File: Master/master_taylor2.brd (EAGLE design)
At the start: 67.9 x 65.1 mm, 47 parts, among them J1 ISP, K1 653002114822, K2 653002114822, K3 653002114822, K4 653002114822, U1 ATMEGA128RFA1, U2 TPS73633-DBVT, U3 ULN2003ADR, Y1 16MHz

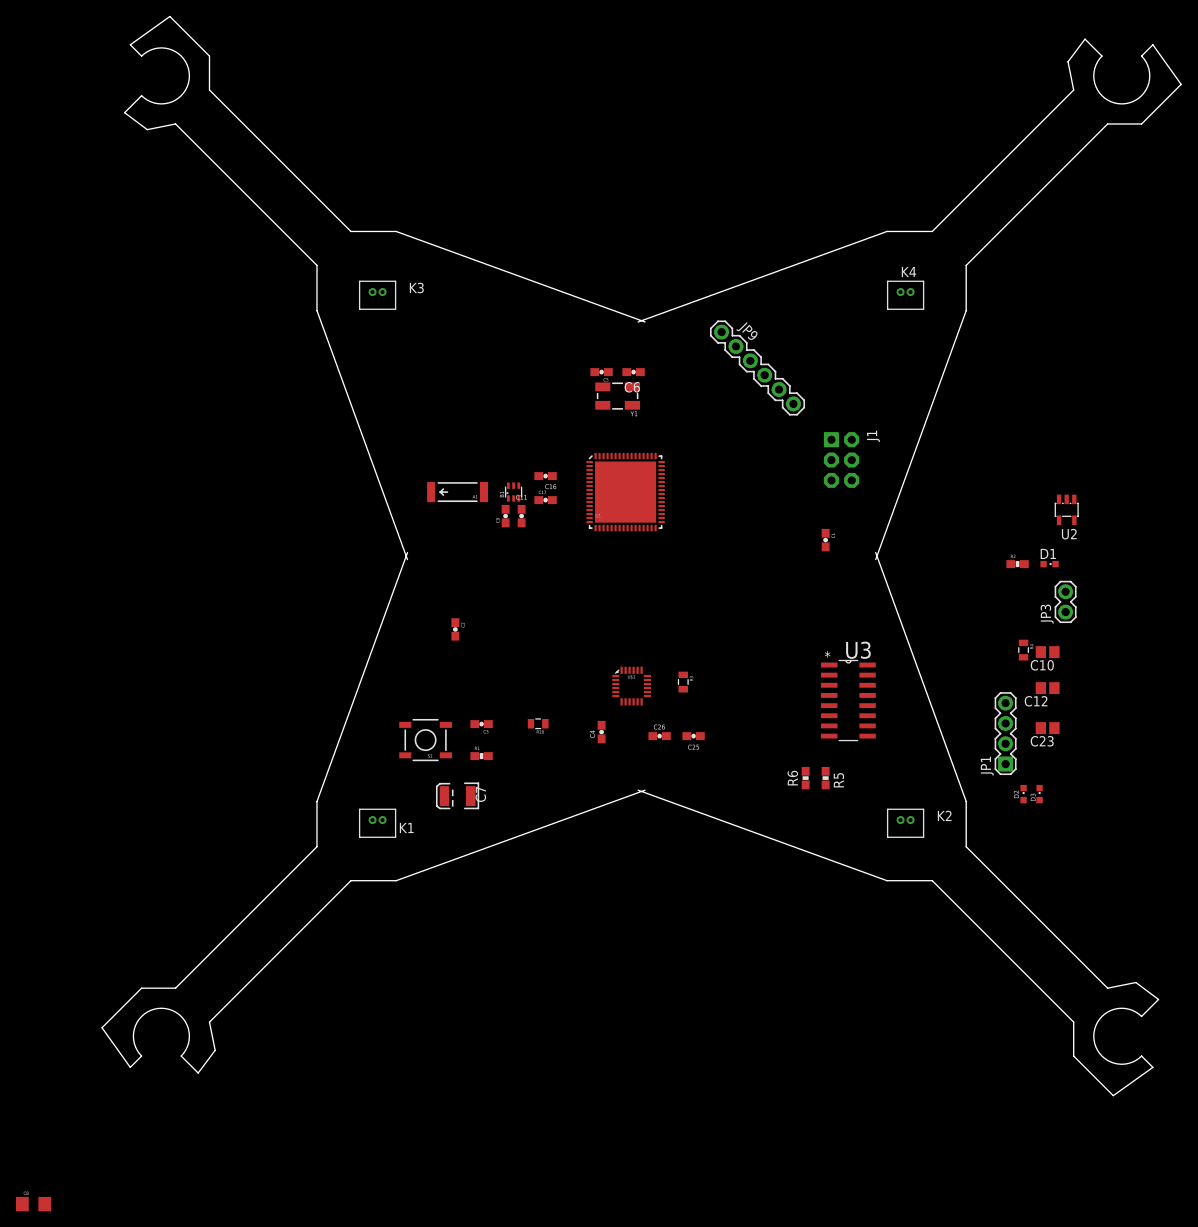
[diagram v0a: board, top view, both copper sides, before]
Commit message: Version 2 routed
Layed out crystal and antenna in accordance with the Cult of Sparkfun
Added keepouts to IMU because of Jorge's recommendation
Added keepout to antenna to not disturb the ether wind.
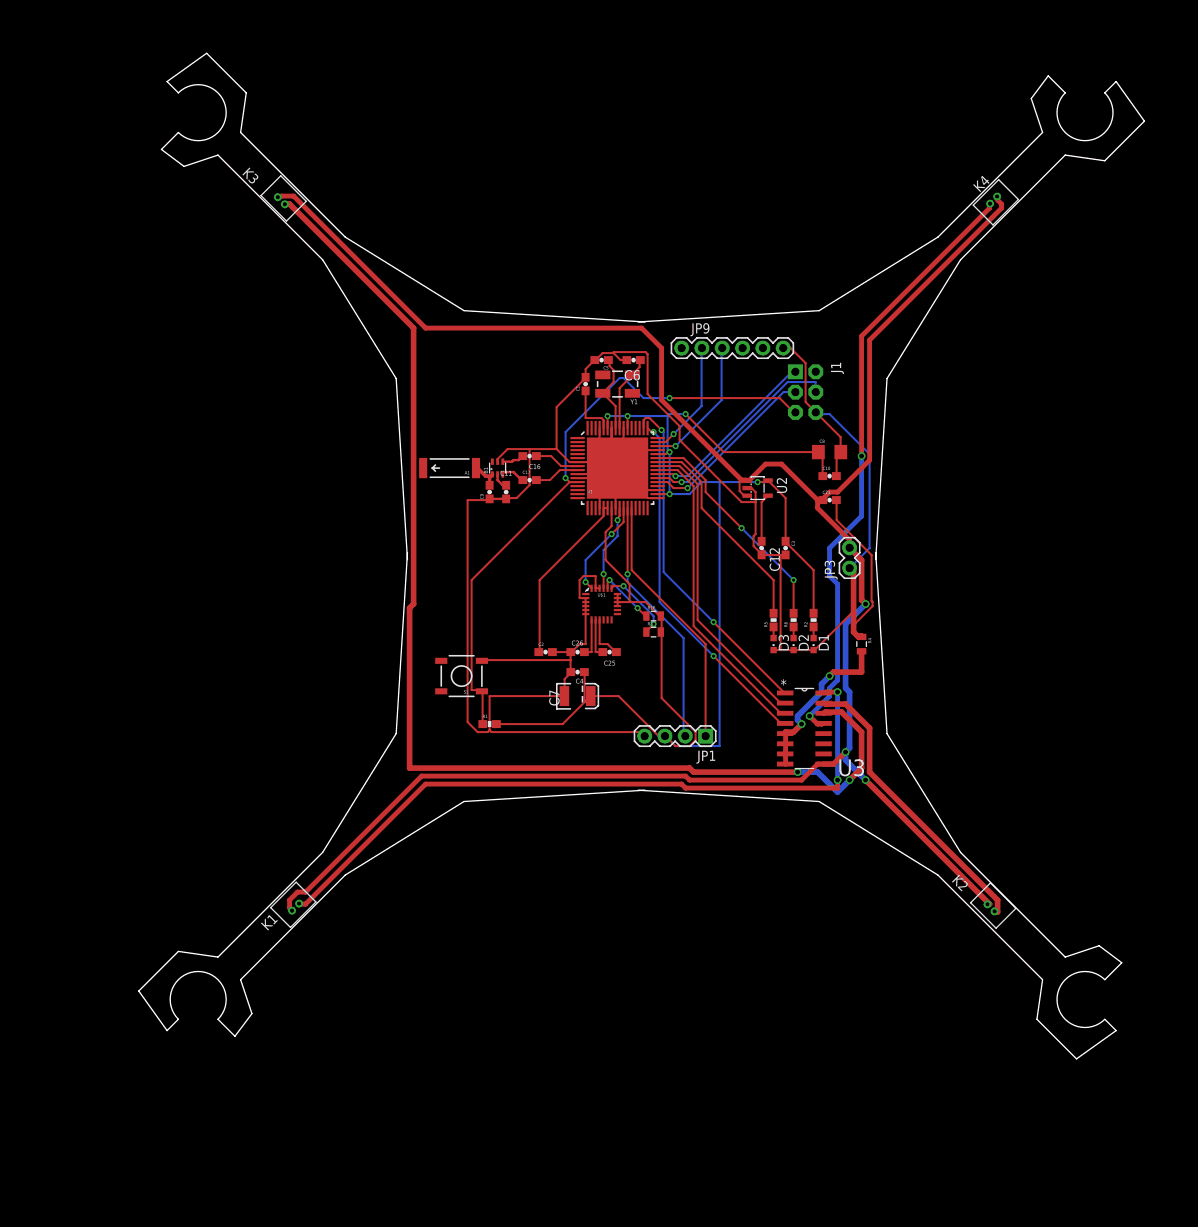
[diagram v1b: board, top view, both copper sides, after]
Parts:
- C10, C12, C23: device resistor:C0805 -> SparkFun-Capacitors:0603-CAP
- D3: value WHITE -> GREEN
- JP1: value Debuger -> Debugger
- U1: device SparkFun-DigitalIC:QFN-64 -> master_devon:QFN-64
- moved C8 136.9 mm to (23.5, 13.0)
- moved C3 43.9 mm to (18.0, 1.00), turned to 270 degrees
- moved C12 39.8 mm to (15.0, 1.00), turned to 270 degrees
- moved C23 39.4 mm to (23.5, 7.00), turned to 0 degrees
- moved U2 38.7 mm to (14.5, 8.50), turned to 270 degrees
- moved D3 38.2 mm to (16.5, -11.0), turned to 180 degrees
- moved JP1 37.7 mm to (8.00, -22.5), turned to 180 degrees
- moved C1 35.8 mm to (-7.00, 21.5), turned to 90 degrees
- moved C10 35.0 mm to (23.5, 10.0), turned to 0 degrees
- moved D2 34.3 mm to (19.0, -11.0), turned to 180 degrees
- moved D1 31.1 mm to (21.5, -11.0), turned to 180 degrees
- moved JP3 27.6 mm to (26.0, -1.50)
- moved R2 26.4 mm to (21.5, -8.00), turned to 90 degrees
- moved R5 20.8 mm to (16.5, -8.00), turned to 90 degrees
- moved R4 20.3 mm to (27.5, -11.0)
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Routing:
- net GND: track 0.00 -> 325.3 mm
- net VBAT: track 0.00 -> 281.3 mm, vias 0 -> 3
- net 3.3V: track 0.00 -> 191.8 mm, vias 0 -> 6
- net N$31: track 0.00 -> 147.0 mm, vias 0 -> 2
- net N$29: track 0.00 -> 87.5 mm, vias 0 -> 2
- net RESET: track 0.00 -> 77.4 mm, vias 0 -> 2
- net N$32: track 0.00 -> 76.4 mm, vias 0 -> 2
- net PE3: track 0.00 -> 44.5 mm, vias 0 -> 2
- net PE4: track 0.00 -> 43.3 mm, vias 0 -> 2
- net PB4: track 0.00 -> 38.8 mm
- net PB5: track 0.00 -> 38.2 mm
- net N$30: track 0.00 -> 37.0 mm
- net TX1: track 0.00 -> 32.3 mm
- net RX1: track 0.00 -> 31.6 mm, vias 0 -> 1
- net PB7: track 0.00 -> 28.3 mm, vias 0 -> 2
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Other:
- board size 67.9 x 65.1 mm -> 63.3 x 60.5 mm

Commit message: Changed outline a bit to reduce weight
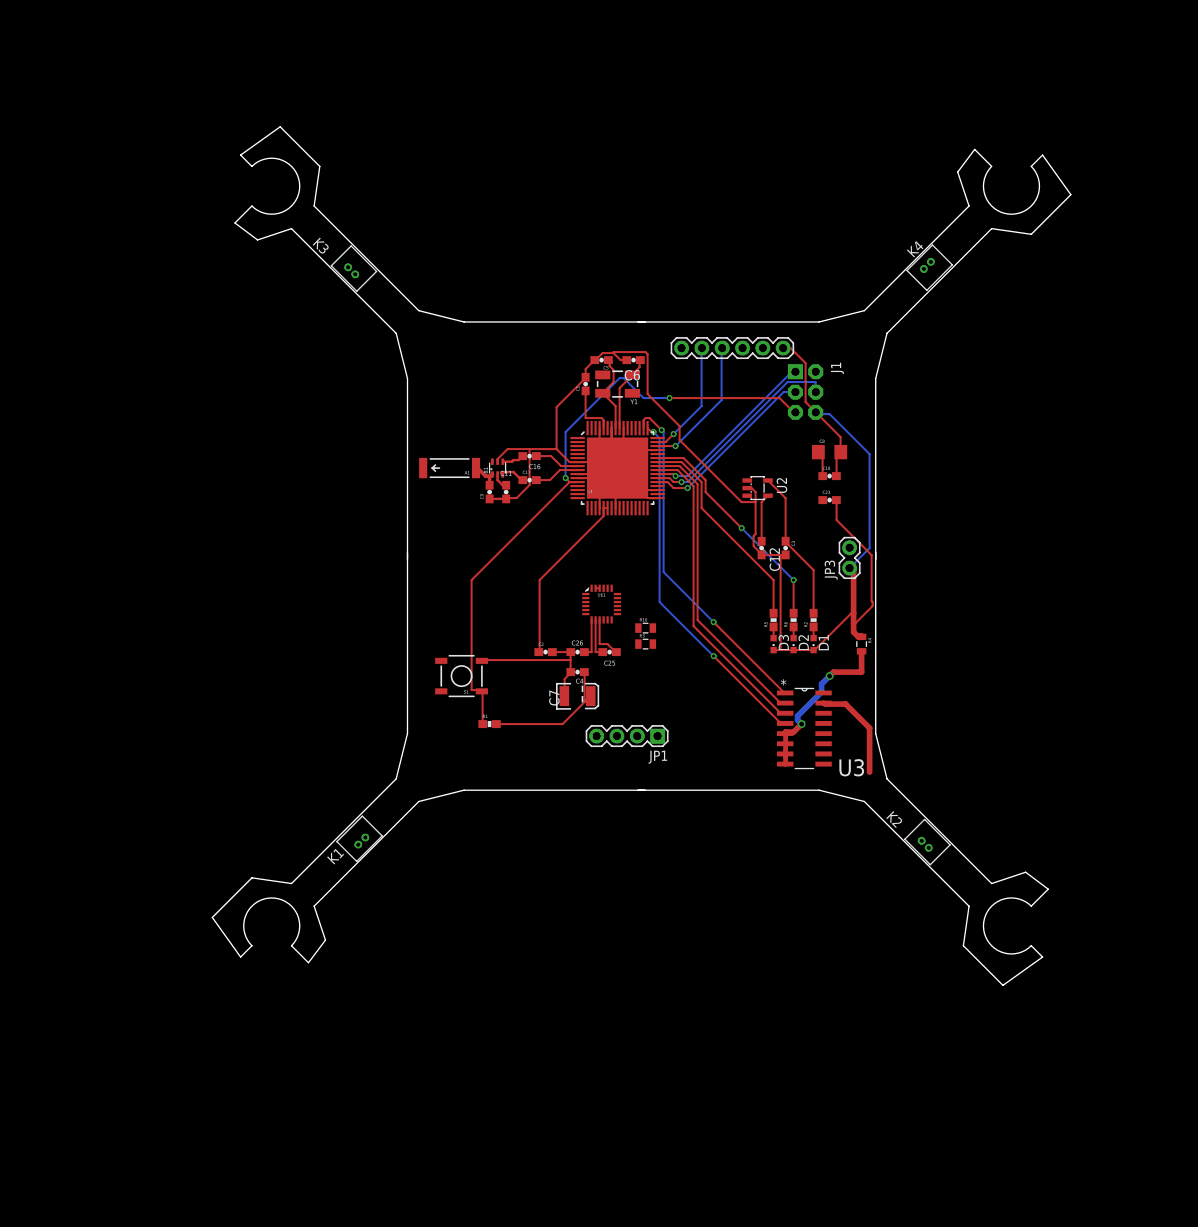
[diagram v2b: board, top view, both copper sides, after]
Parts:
- moved K3 12.4 mm to (-36.2, 35.7)
- moved K1 11.7 mm to (-35.0, -35.6)
- moved K4 11.6 mm to (35.7, 36.3)
- moved K2 11.4 mm to (35.5, -36.0)
- moved JP1 6.00 mm to (2.00, -22.5)
- moved R10 1.80 mm to (0.50, -9.00)
- moved R3 1.80 mm to (0.50, -11.0)
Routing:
- net VBAT: track 281.3 -> 0.00 mm, vias 3 -> 0
- net 3.3V: track 191.8 -> 39.2 mm, vias 6 -> 0
- net N$31: track 147.0 -> 0.00 mm, vias 2 -> 0
- net N$29: track 87.5 -> 0.00 mm, vias 2 -> 0
- net GND: track 325.3 -> 243.1 mm
- net N$32: track 76.4 -> 0.00 mm, vias 2 -> 0
- net TX1: track 32.3 -> 0.00 mm
- net RX1: track 31.6 -> 0.00 mm, vias 1 -> 0
- net N$30: track 37.0 -> 12.5 mm
- net SDA: track 12.3 -> 0.00 mm, vias 2 -> 0
- net SCL: track 10.9 -> 0.00 mm, vias 2 -> 0
- net N$23: track 9.45 -> 0.00 mm, vias 2 -> 0
- net N$24: track 7.74 -> 0.00 mm, vias 2 -> 0
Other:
- board size 63.3 x 60.5 mm -> 54.1 x 51.3 mm

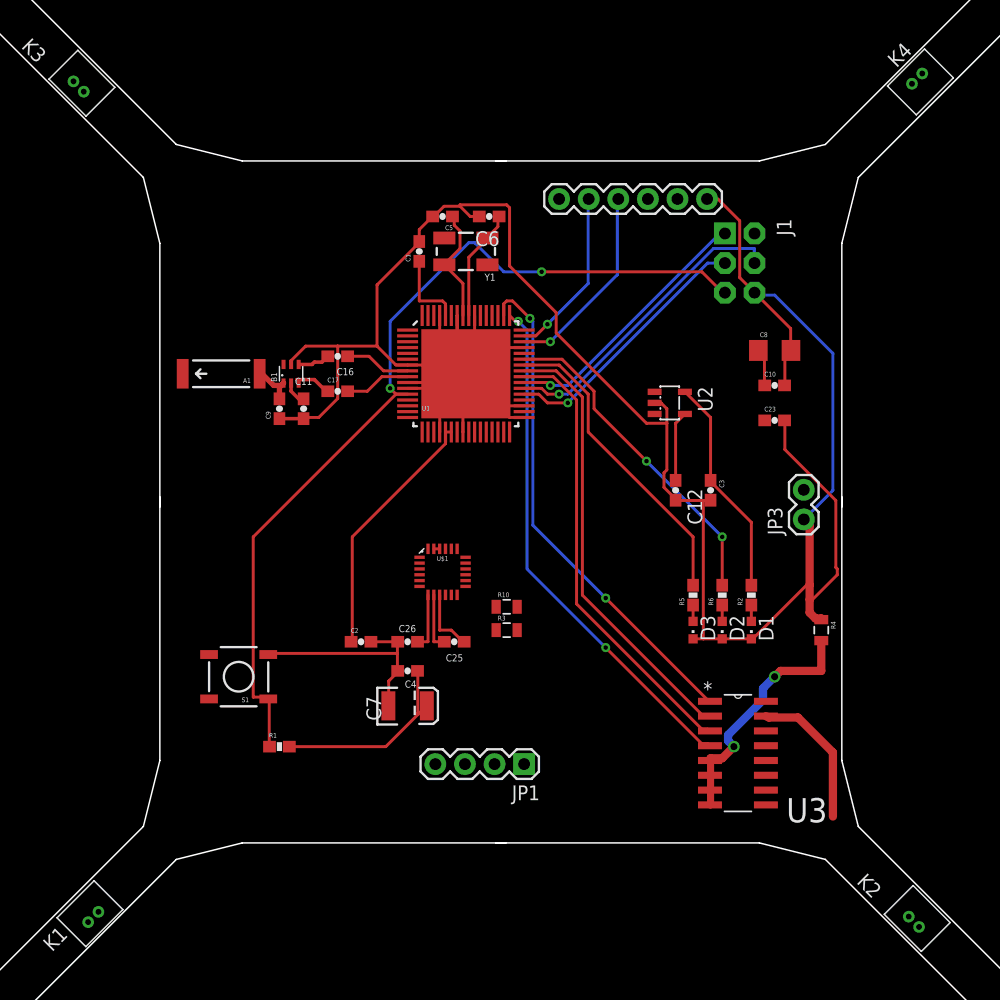
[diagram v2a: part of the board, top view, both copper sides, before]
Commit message: Hand routed motors
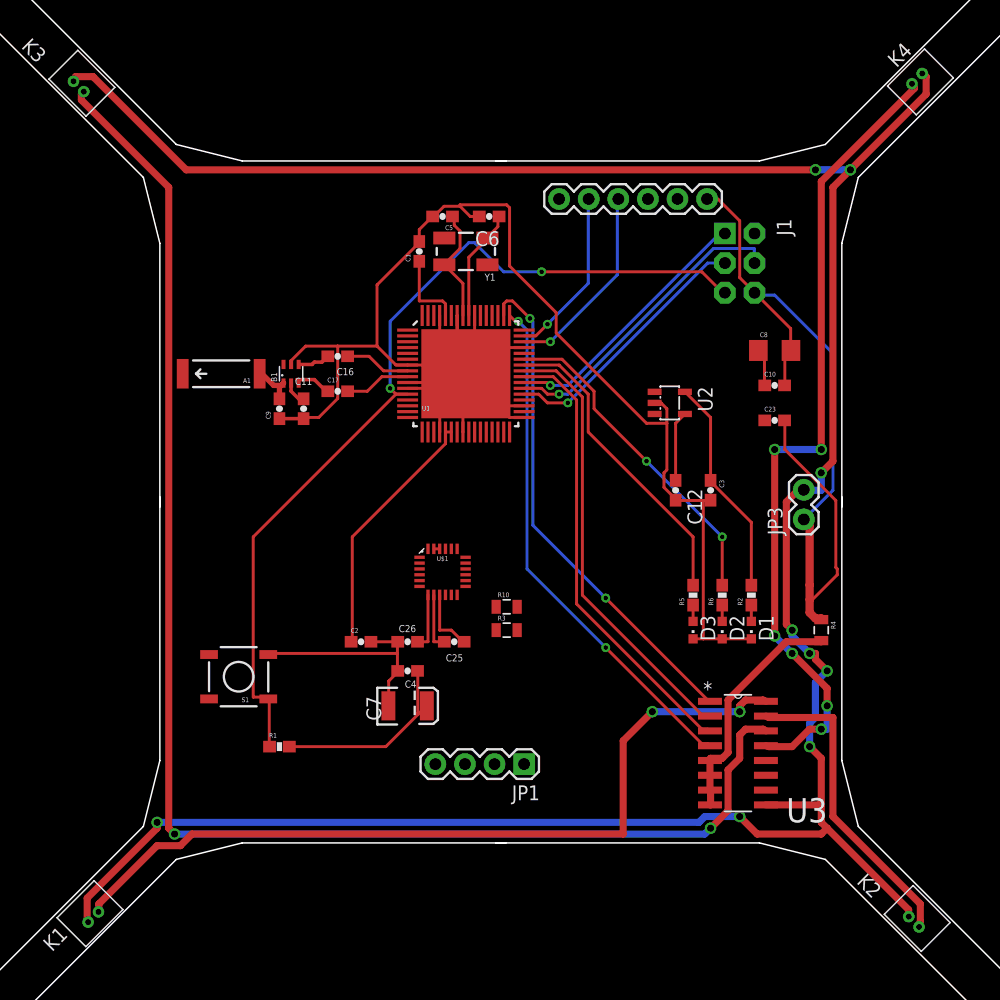
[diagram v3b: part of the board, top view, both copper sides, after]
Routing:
- net VBAT: track 0.00 -> 230.0 mm, vias 0 -> 9
- net N$31: track 0.00 -> 124.8 mm, vias 0 -> 2
- net N$32: track 0.00 -> 70.5 mm, vias 0 -> 6
- net N$29: track 0.00 -> 70.2 mm, vias 0 -> 2
- net N$30: track 12.5 -> 26.9 mm
- net GND: track 243.1 -> 236.6 mm
- net N$12: track 21.4 -> 20.4 mm, vias 2 -> 0

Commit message: More tweaks, I don't even remember what I did
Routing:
- net 3.3V: track 39.2 -> 179.1 mm, vias 0 -> 8
- net GND: track 236.6 -> 276.0 mm, vias 0 -> 1
- net TX1: track 0.00 -> 30.0 mm
- net RX1: track 0.00 -> 29.7 mm
- net VBAT: track 230.0 -> 252.8 mm
- net SDA: track 0.00 -> 21.9 mm, vias 0 -> 2
- net SCL: track 0.00 -> 10.9 mm
- net N$23: track 0.00 -> 8.98 mm
- net N$24: track 0.00 -> 8.84 mm
